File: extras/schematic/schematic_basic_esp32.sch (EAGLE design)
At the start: 18 parts, among them U1 SI4735-D60-GU

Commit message: SI47XX Arduino Library
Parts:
- removed B1: ARDUINO_PRO_MINI, SparkFun-Boards:ARDUINO_PRO_MINI
- added ESP32: See your ESP32 pinout, SparkFun-Boards:ESP32_THING_WO_ANT_KEEPOUT
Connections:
- net GND: now also ESP32.GND@21; no longer B1.GND@2
- net N$1: now also ESP32.25; no longer B1.12
- net N$2: now also ESP32.21; no longer B1.A4
- net SDA: now also ESP32.19, ESP32.22; no longer B1.A5
- net VCC: now also ESP32.3V3@5; no longer B1.VCC
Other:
- moved on the sheet: AM, C1, C2, C3, C4, C5, C6, C7, C8, FM, J1, L1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

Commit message: SI473X Arduino Library
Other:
- note added: "Optional"
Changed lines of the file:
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@@
 <sheet>
 <plain>
+<rectangle x1="-129.54" y1="180.34" x2="-114.3" y2="195.58" layer="205"/>
+<text x="-127" y="198.12" size="1.778" layer="205">Optional</text>
 </plain>
 <instances>

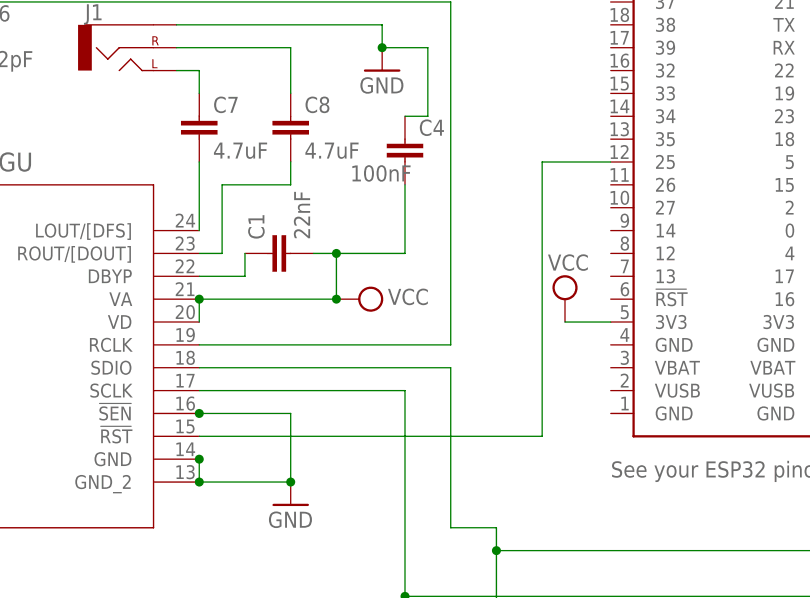
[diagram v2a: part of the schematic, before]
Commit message: SI473X Arduino Library
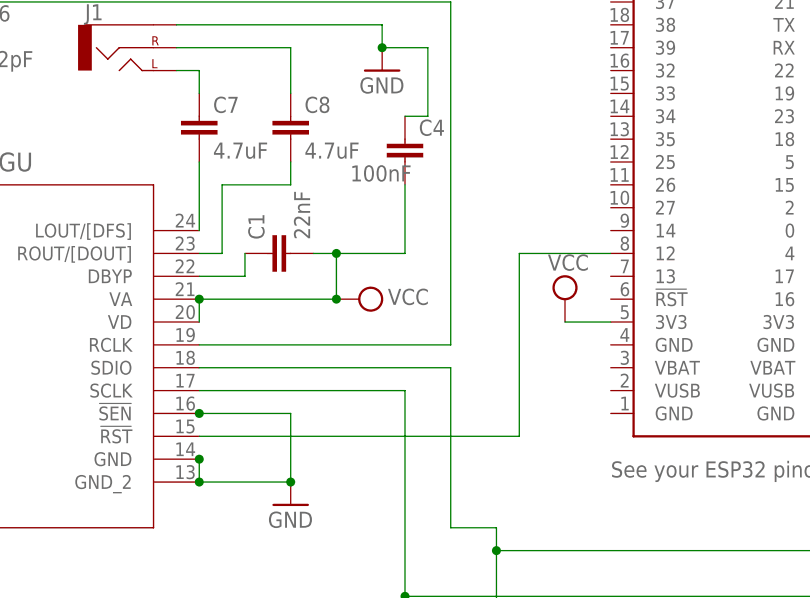
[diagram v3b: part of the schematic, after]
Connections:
- net N$1: now also ESP32.12; no longer ESP32.25
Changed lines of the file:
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@@
 <segment>
 <pinref part="U1" gate="A" pin="!RST"/>
-<wire x1="-60.96" y1="139.7" x2="-22.86" y2="139.7" width="0.1524" layer="91"/>
-<wire x1="-22.86" y1="139.7" x2="-22.86" y2="170.18" width="0.1524" layer="91"/>
-<pinref part="ESP32" gate="G$1" pin="25"/>
-<wire x1="-22.86" y1="170.18" x2="-15.24" y2="170.18" width="0.1524" layer="91"/>
+<wire x1="-60.96" y1="139.7" x2="-25.4" y2="139.7" width="0.1524" layer="91"/>
+<pinref part="ESP32" gate="G$1" pin="12"/>
+<wire x1="-25.4" y1="139.7" x2="-25.4" y2="160.02" width="0.1524" layer="91"/>
+<wire x1="-25.4" y1="160.02" x2="-15.24" y2="160.02" width="0.1524" layer="91"/>
 </segment>
 </net>
